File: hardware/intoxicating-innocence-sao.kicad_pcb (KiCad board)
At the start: 2 copper layers, 0 parts

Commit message: Add PCB  outline
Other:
- board outline added: 36 x 32 mm
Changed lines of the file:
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@@
 	(property "PROJECT_REVISION" "1")
 	(property "PROJECT_URL" "https://github.com/kantoniak/intoxicating-innocence-sao")
+	(gr_arc
+		(start 82 100)
+		(mid 100 82)
+		(end 118 100)
+		(stroke
+			(width 0)
+			(type default)
+		)
+		(layer "Edge.Cuts")
+	)
+	(gr_line
+		(start 82 107.313708)
+		(end 82 100)
+		(stroke
+			(width 0)
+			(type default)
+		)
+		(layer "Edge.Cuts")
+	)
+	(gr_line
+		(start 88.686292 114)
+		(end 82 107.313708)
+		(stroke
+			(width 0)
+			(type default)
+		)
+		(layer "Edge.Cuts")
+	)
+	(gr_line
+		(start 111.313708 114)
+		(end 88.686292 114)
+		(stroke
+			(width 0)
+			(type default)
+		)
+		(layer "Edge.Cuts")
+	)
+	(gr_line
+		(start 118 100)
+		(end 118 107.313708)
+		(stroke
+			(width 0)
+			(type default)
+		)
+		(layer "Edge.Cuts")
+	)
+	(gr_line
+		(start 118 107.313708)
+		(end 111.313708 114)
+		(stroke
+			(width 0)
+			(type default)
+		)
+		(layer "Edge.Cuts")
+	)
+	(point
+		(at 100.00 100.00)
+		(size 1)
+		(layer "F.CrtYd")
+	)
+	(group ""
+		(members "1a00966c-e4cf-4aeb-a0c1-7f8dbd2b5766" "2909549f-a129-48a3-b18f-0546b8939bec"
+			"895ad8c0-1a98-44f7-afaa-3ebda2a3a05a" "8c57d2d3-fb16-458a-b846-a2680969f1eb"
+			"ead3cd93-434e-4455-a599-2dcdadc07b79" "fbfffde6-6854-4b22-8358-131de7647bb9"
+		)
+	)
 	(embedded_fonts no)
 )

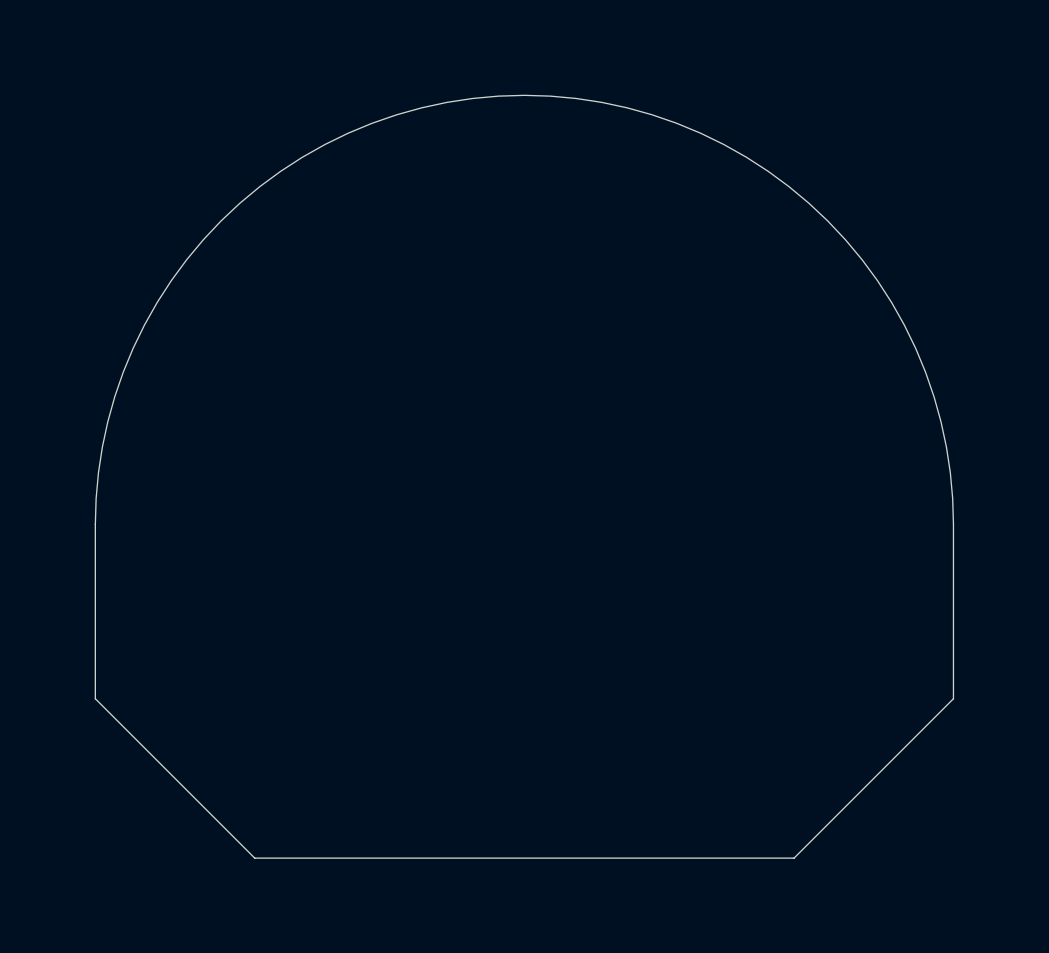
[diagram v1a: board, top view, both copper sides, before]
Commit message: Place geometry-informing components on the PCB
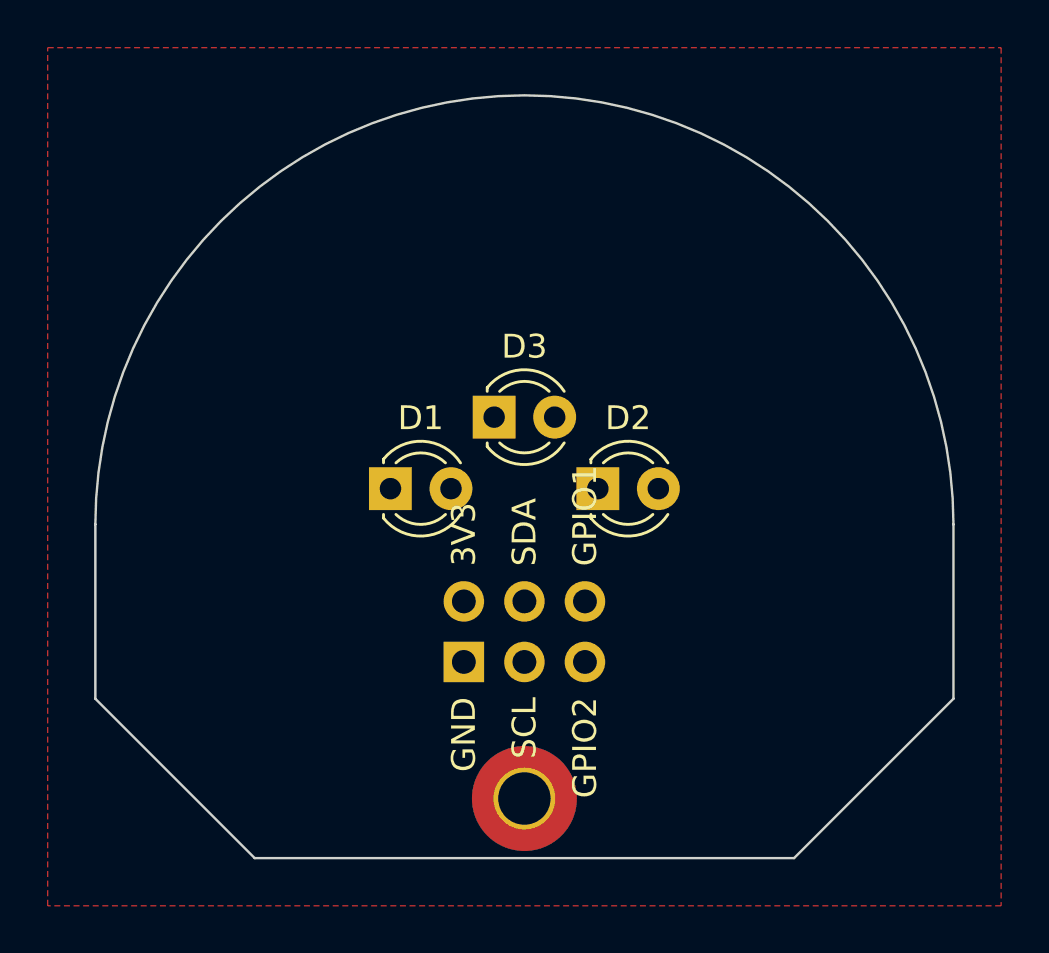
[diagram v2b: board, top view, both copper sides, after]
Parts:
- added D1: RED, LED_THT:LED_D3.0mm, F.Cu at (94.4, 98.5)
- added D2: RED, LED_THT:LED_D3.0mm, F.Cu at (103.1, 98.5)
- added D3: RED, LED_THT:LED_D3.0mm, F.Cu at (98.7, 95.5)
- added J1: SAO, kantoniak-kicad:SAO_Header_Addon_Side, B.Cu at (97.5, 105.8)
- added REF**: MountingHole_2.2mm_M2_Pad_TopBottom, MountingHole:MountingHole_2.2mm_M2_Pad_TopBottom, F.Cu at (100.0, 111.5)
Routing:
- added copper zone on F.Cu, net GND
